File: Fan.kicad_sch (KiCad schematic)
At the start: 0 parts

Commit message: Sheet complete for the fan
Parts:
- added C84, C85: 100nF/50V, A_HDJ_Library:C_0402_1005Metric, symbol Device:C
- added D26, D27: 1N5819WS, A_HDJ_Library:D_SOD-323, symbol Diode:1N5819WS
- added JP79: SolderJumper_2_Open, Jumper:SolderJumper-2_P1.3mm_Bridged_RoundedPad1.0x1.5mm, symbol Jumper:SolderJumper_2_Open
- added M2, M78: Fan_4pin, symbol Motor:Fan_4pin
- added R63: 10k/1%, A_HDJ_Library:R_0402_1005Metric, symbol Device:R
- added R64, R65, R72, R74, R75: 4.7k/1%, A_HDJ_Library:R_0402_1005Metric, symbol Device:R
- added R66, R67, R68, R70: 21.5k/1%, A_HDJ_Library:R_0402_1005Metric, symbol Device:R
- added R69, R71: 100/1%, A_HDJ_Library:R_0402_1005Metric, symbol Device:R
- added R74: 0/1%, Resistor_SMD:R_0201_0603Metric, symbol Device:R
- added TH78: Thermistor_NTC, symbol Device:Thermistor_NTC
- added TP11, TP12: TestPoint, symbol Connector:TestPoint
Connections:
- new net: D26.2 (A), M78.3 (Tacho), R68.2, R72.2
- new net: C85.1, D27.1 (K), M2.2 (+), R74.1, R74.2, R75.2
- new net: D27.2 (A), M2.3 (Tacho), R70.2, R74.2
- new net: JP79.2 (B), R63.1, TH78.1
- new net: M78.4 (PWM), R69.2
- new net: M2.4 (PWM), R71.2
- new net +12V: R75.1
- new net +3.3V: R63.2, R64.2, R65.2
- new net +5V: C84.1, D26.1 (K), M78.2 (+), R72.1, R74.1
- new net FAN_1_PWM: R69.1, TP12.1
- new net FAN_1_TAC: R64.1, R66.2, R68.1, TP11.1
- new net FAN_2_PWM: R71.1
- new net FAN_2_TAC: R65.1, R67.2, R70.1
- new net GND: C84.2, C85.2, M2.1 (-), M78.1 (-), R66.1, R67.1, TH78.2
- new net TEMP: JP79.1 (A)
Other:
- note added: "LattePanda Mu has integrated pull-up resistors (which we will not be using J.S. 2026)"
- note added: "Reserved for 12V fan FAN_TAC input ony allows 3.3v level"

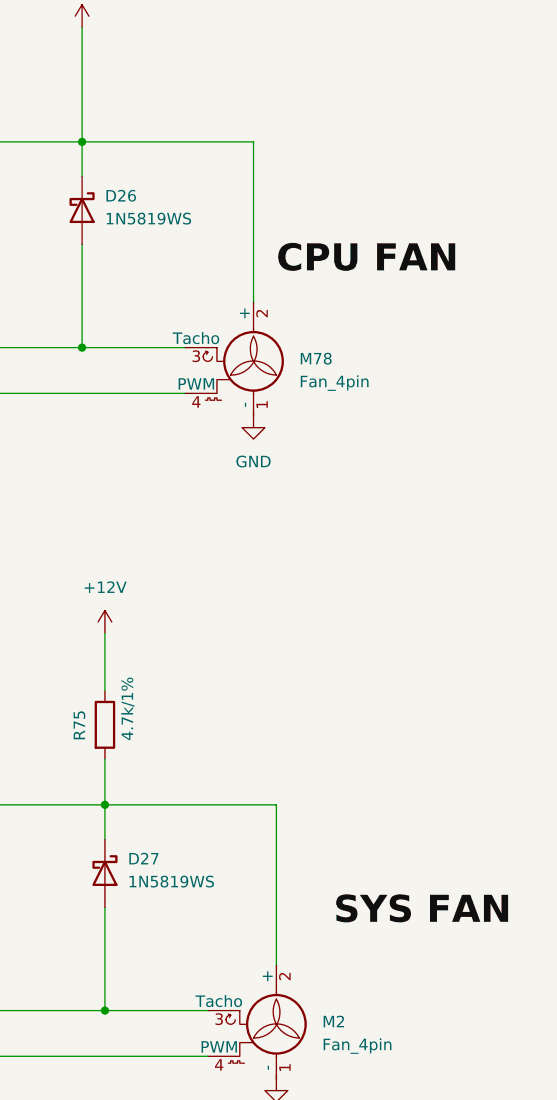
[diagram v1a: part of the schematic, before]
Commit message: Connected the hierarchal sheets together for the fan and the Mu moduls on the main sheet level and also added the label for the extrnal temp sensor for thermistor
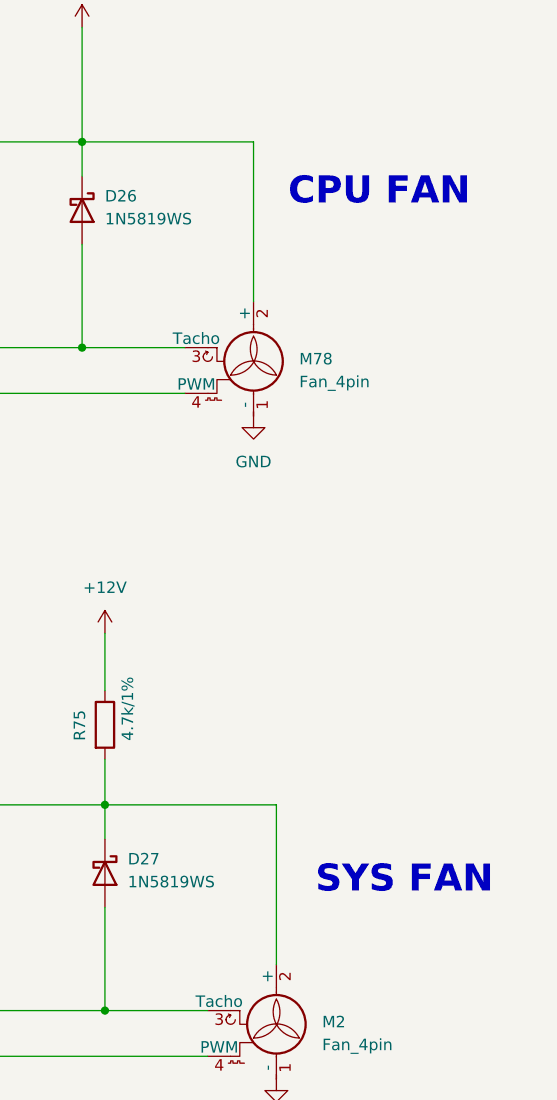
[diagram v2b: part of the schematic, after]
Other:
- note added: "CPU FAN"
- note added: "SYS FAN"
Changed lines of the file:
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@@
+		)
+	)
+	(text "SYS FAN"
+		(exclude_from_sim no)
+		(at 268.224 113.792 0)
+		(effects
+			(font
+				(size 3 3)
+				(thickness 0.6)
+				(bold yes)
+				(color 0 0 255 1)
+			)
 		)
 	)
@@
 			(font
 				(size 1.27 1.27)
+			)
+		)
+	)
+	(text "CPU FAN"
+		(exclude_from_sim no)
+		(at 265.43 37.338 0)
+		(effects
+			(font
+				(size 3 3)
+				(thickness 0.6)
+				(bold yes)
+				(color 0 0 255 1)
 			)
 		)
@@
 		)
 	)
-	(label "SYS FAN"
-		(at 260.35 119.38 0)
-		(effects
-			(font
-				(size 3 3)
-				(thickness 0.6)
-				(bold yes)
-				(color 0 0 255 1)
-			)
-			(justify left bottom)
-		)
-	)
-	(label "CPU FAN"
-		(at 254 46.99 0)
-		(effects
-			(font
-				(size 3 3)
-				(thickness 0.6)
-				(bold yes)
-				(color 0 0 255 1)
-			)
-			(justify left bottom)
-		)
-	)

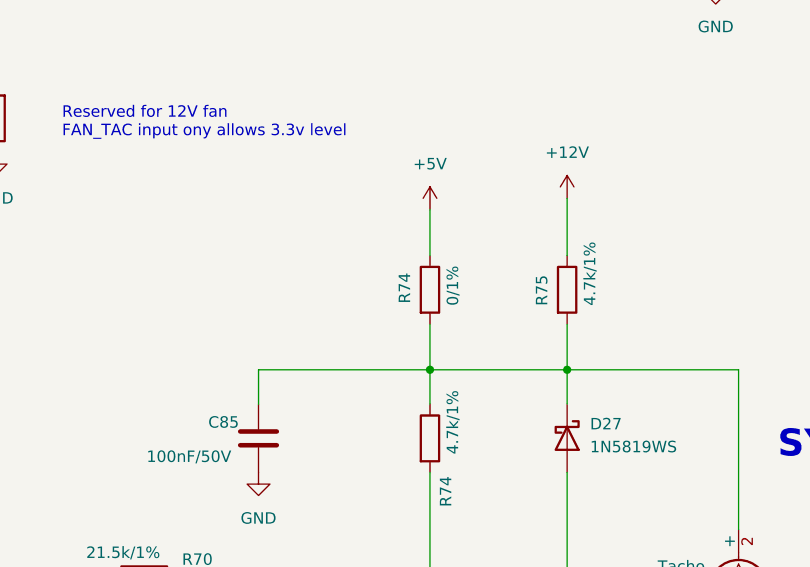
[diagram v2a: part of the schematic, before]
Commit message: Fixed annotation errors duplicate designators on passive components R11 and J15 so that schematic could be imported into pcb. There might be some missing footprints... starting that investigation
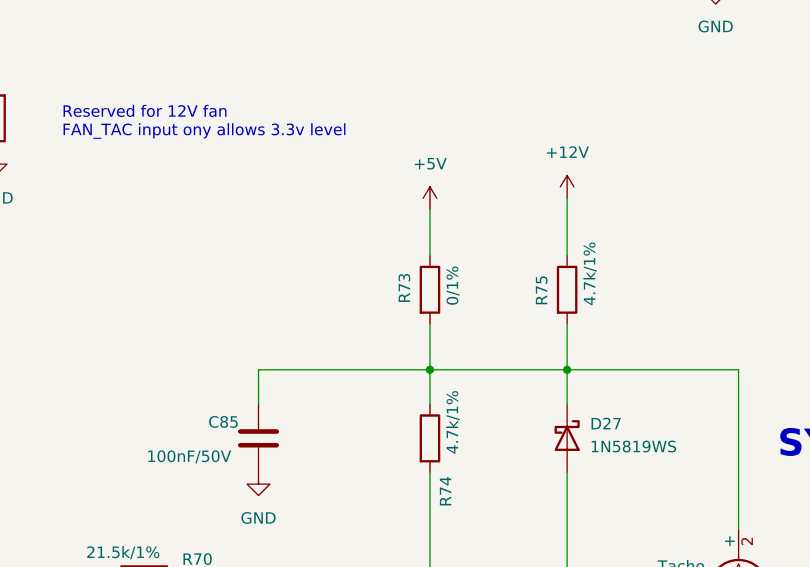
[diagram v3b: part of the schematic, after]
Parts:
- renumbered R74 to R73
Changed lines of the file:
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@@
 		(in_pos_files yes)
 		(dnp no)
-		(property "Reference" "R74"
+		(property "Reference" "R73"
 			(at 216.916 98.044 90)
 			(show_name no)
@@
 			(project "Carrier_Board"
 				(path "/e768274e-12f3-4f83-96f6-abb7638e0bc1/db5534e0-ad9a-443b-b9b9-b696f6fb2c85"
-					(reference "R74")
+					(reference "R73")
 					(unit 1)
 				)

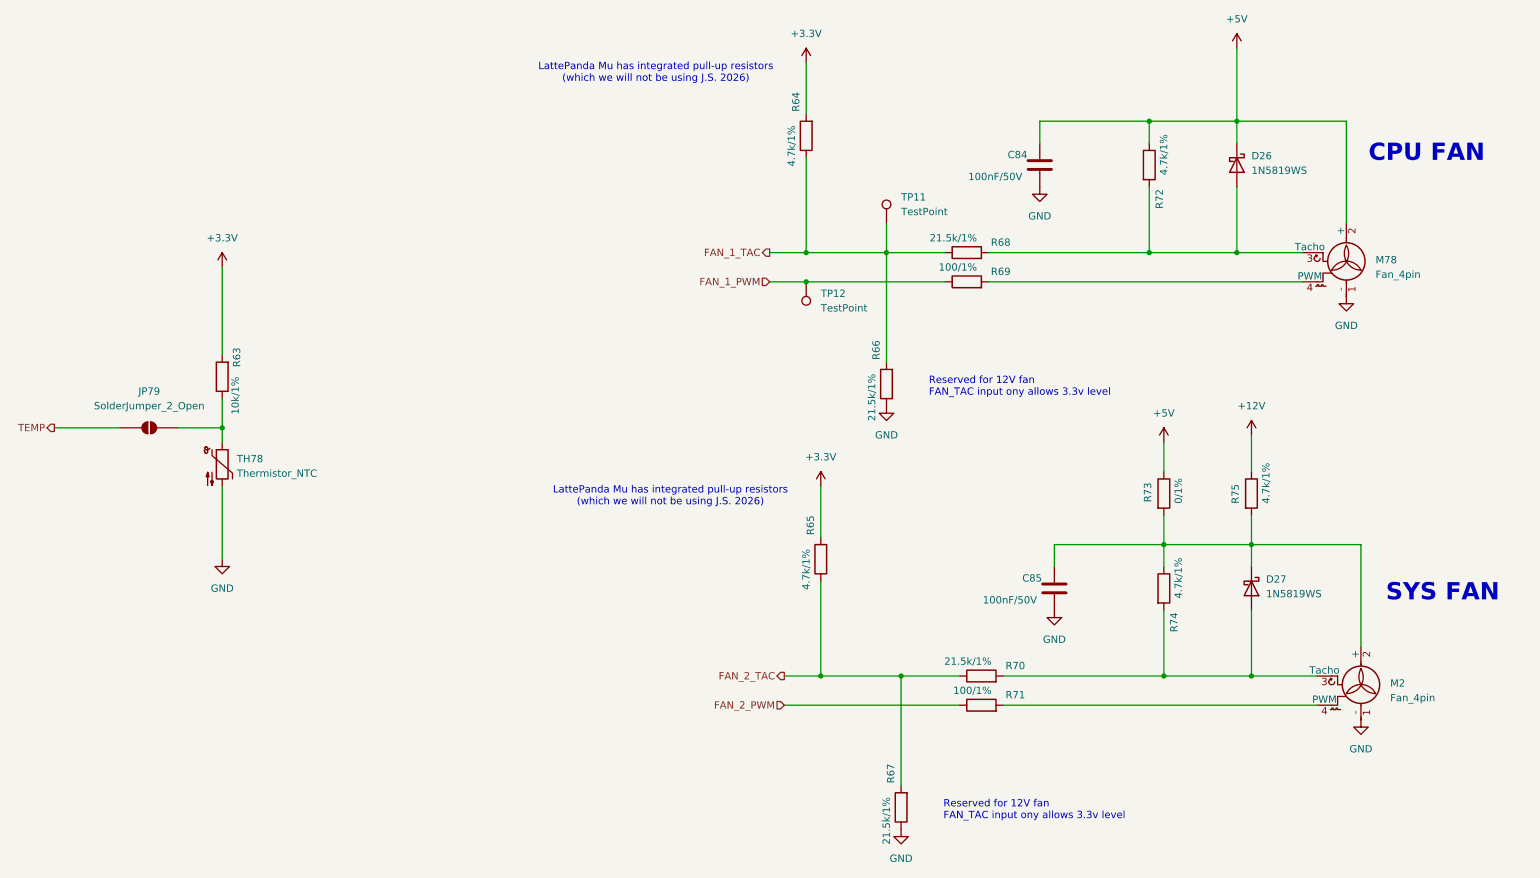
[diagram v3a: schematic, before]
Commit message: Updated all the footprints into the pcb editor but all the designator numbers have changed... I have tp go back and fix each one
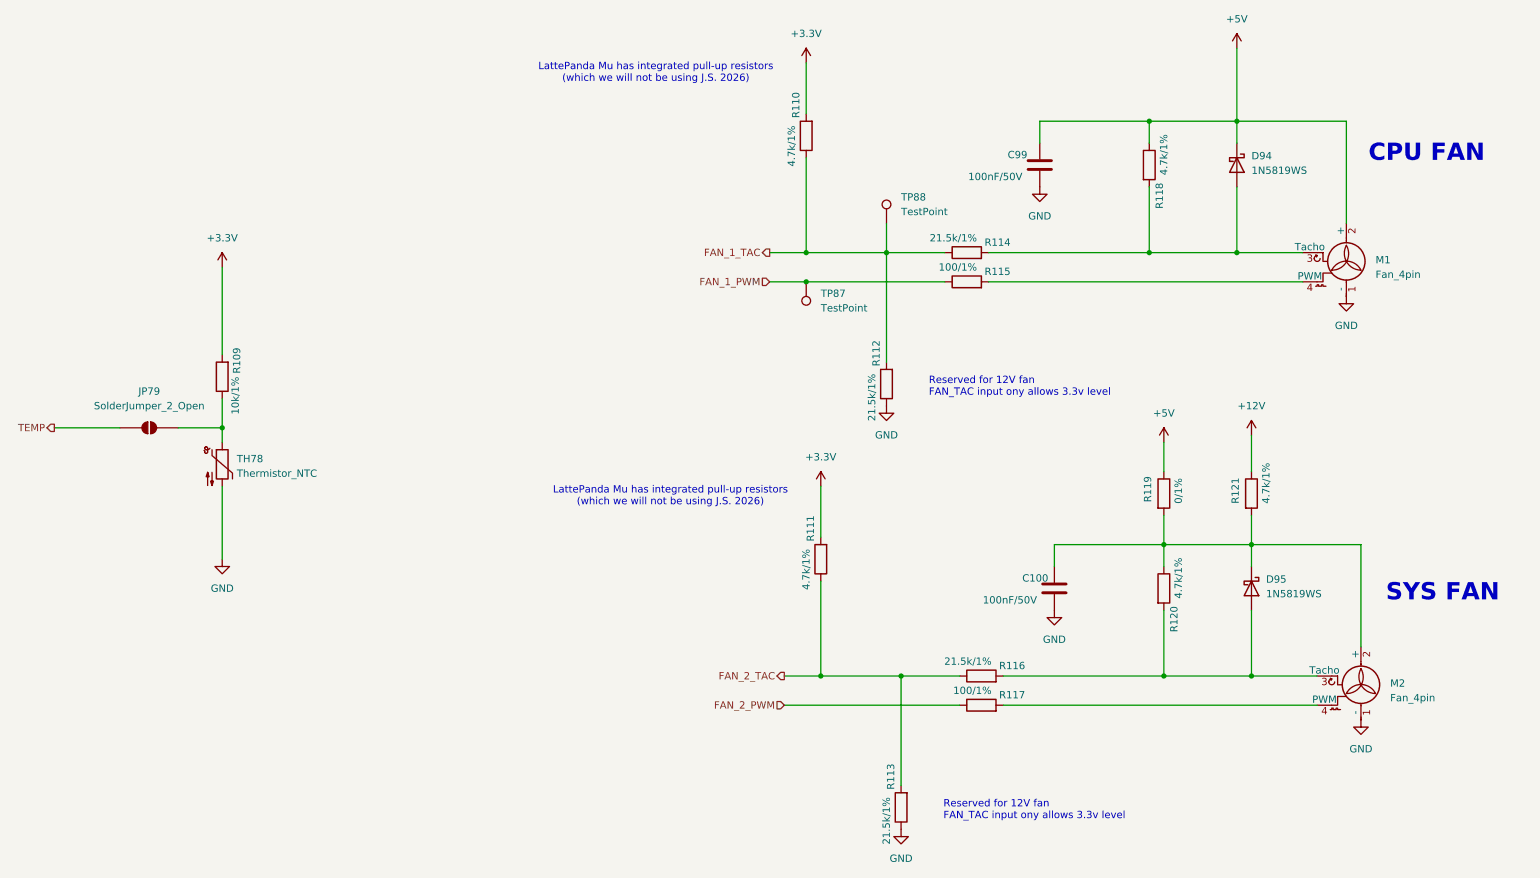
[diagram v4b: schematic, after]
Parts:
- M1: renamed from M78; footprint (none) -> A_HDJ_Library:JST_PH_B4B-PH-K_1x04_P2.00mm_Vertical
- M2: footprint (none) -> A_HDJ_Library:JST_PH_B4B-PH-K_1x04_P2.00mm_Vertical
- TH78: footprint (none) -> A_HDJ_Library:R_0603_1608Metric
- TP87: renamed from TP12; footprint (none) -> A_HDJ_Library:TestPoint_Pad_D1.5mm
- TP88: renamed from TP11; footprint (none) -> A_HDJ_Library:TestPoint_Pad_D1.5mm
- renumbered C85 to C100, C84 to C99, D26 to D94, D27 to D95, R63 to R109, R64 to R110, R65 to R111, R66 to R112, R67 to R113, R68 to R114, R69 to R115, R70 to R116, R71 to R117, R72 to R118, R73 to R119, R74 to R120, R75 to R121

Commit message: Designators in fans restored
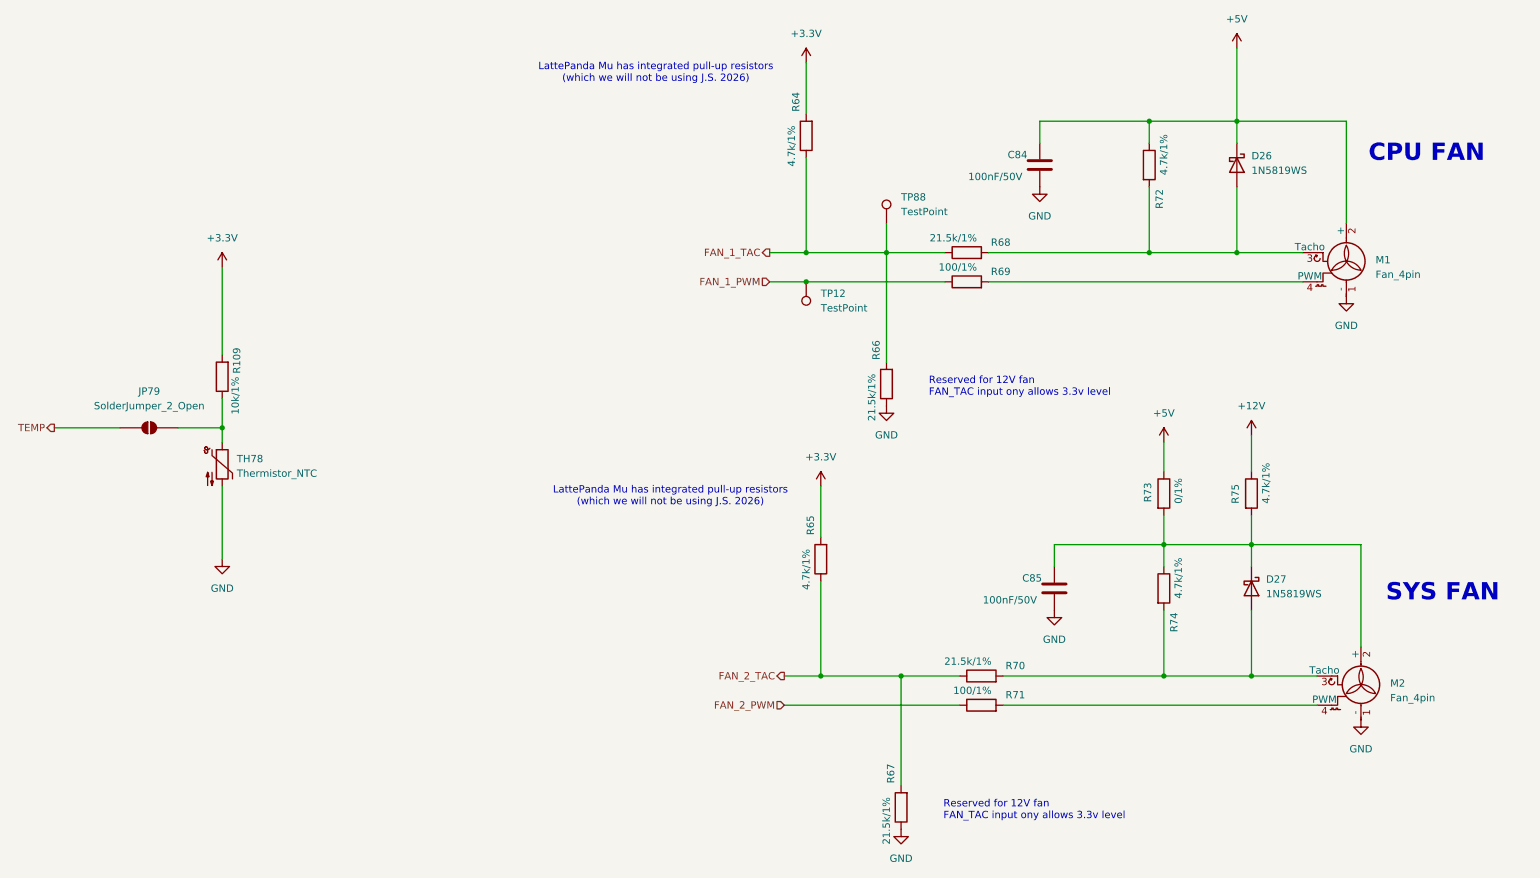
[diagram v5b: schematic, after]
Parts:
- renumbered C99 to C84, C100 to C85, D94 to D26, D95 to D27, R110 to R64, R111 to R65, R112 to R66, R113 to R67, R114 to R68, R115 to R69, R116 to R70, R117 to R71, R118 to R72, R119 to R73, R120 to R74, R121 to R75, TP87 to TP12
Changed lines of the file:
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@@
 		(in_pos_files yes)
 		(dnp no)
-		(property "Reference" "R114"
+		(property "Reference" "R68"
 			(at 193.04 52.832 90)
 			(show_name no)
@@
 			(project "Carrier_Board"
 				(path "/e768274e-12f3-4f83-96f6-abb7638e0bc1/db5534e0-ad9a-443b-b9b9-b696f6fb2c85"
-					(reference "R114")
+					(reference "R68")
 					(unit 1)
 				)
@@
 		(in_pos_files yes)
 		(dnp no)
-		(property "Reference" "R120"
+		(property "Reference" "R74"
 			(at 221.488 120.65 90)
 			(show_name no)
@@
 			(project "Carrier_Board"
 				(path "/e768274e-12f3-4f83-96f6-abb7638e0bc1/db5534e0-ad9a-443b-b9b9-b696f6fb2c85"
-					(reference "R120")
+					(reference "R74")
 					(unit 1)
 				)
@@
 		(in_pos_files yes)
 		(dnp no)
-		(property "Reference" "R113"
+		(property "Reference" "R67"
 			(at 172.212 143.51 90)
 			(show_name no)
@@
 			(project "Carrier_Board"
 				(path "/e768274e-12f3-4f83-96f6-abb7638e0bc1/db5534e0-ad9a-443b-b9b9-b696f6fb2c85"
-					(reference "R113")
+					(reference "R67")
 					(unit 1)
 				)
@@
 		(in_pos_files yes)
 		(dnp no)
-		(property "Reference" "R110"
+		(property "Reference" "R64"
 			(at 155.702 26.67 90)
 			(show_name no)
@@
 			(project "Carrier_Board"
 				(path "/e768274e-12f3-4f83-96f6-abb7638e0bc1/db5534e0-ad9a-443b-b9b9-b696f6fb2c85"
-					(reference "R110")
+					(reference "R64")
 					(unit 1)
 				)
@@
 		(in_pos_files yes)
 		(dnp no)
-		(property "Reference" "R121"
+		(property "Reference" "R75"
 			(at 232.156 98.298 90)
 			(show_name no)
@@
 			(project "Carrier_Board"
 				(path "/e768274e-12f3-4f83-96f6-abb7638e0bc1/db5534e0-ad9a-443b-b9b9-b696f6fb2c85"
-					(reference "R121")
+					(reference "R75")
 					(unit 1)
 				)
@@
 		(in_pos_files yes)
 		(dnp no)
-		(property "Reference" "R111"
+		(property "Reference" "R65"
 			(at 158.242 100.33 90)
 			(show_name no)
@@
 			(project "Carrier_Board"
 				(path "/e768274e-12f3-4f83-96f6-abb7638e0bc1/db5534e0-ad9a-443b-b9b9-b696f6fb2c85"
-					(reference "R111")
+					(reference "R65")
 					(unit 1)
 				)
@@
 		(in_pos_files yes)
 		(dnp no)
-		(property "Reference" "R118"
+		(property "Reference" "R72"
 			(at 218.948 46.99 90)
 			(show_name no)
@@
 			(project "Carrier_Board"
 				(path "/e768274e-12f3-4f83-96f6-abb7638e0bc1/db5534e0-ad9a-443b-b9b9-b696f6fb2c85"
-					(reference "R118")
+					(reference "R72")
 					(unit 1)
 				)
@@
 		(dnp no)
 		(fields_autoplaced yes)
-		(property "Reference" "D94"
+		(property "Reference" "D26"
 			(at 234.95 37.7824 90)
 			(show_name no)
@@
 			(project "Carrier_Board"
 				(path "/e768274e-12f3-4f83-96f6-abb7638e0bc1/db5534e0-ad9a-443b-b9b9-b696f6fb2c85"
-					(reference "D94")
+					(reference "D26")
 					(unit 1)
 				)
@@
 		(in_pos_files yes)
 		(dnp no)
-		(property "Reference" "R116"
+		(property "Reference" "R70"
 			(at 195.58 126.492 90)
 			(show_name no)
@@
 			(project "Carrier_Board"
 				(path "/e768274e-12f3-4f83-96f6-abb7638e0bc1/db5534e0-ad9a-443b-b9b9-b696f6fb2c85"
-					(reference "R116")
+					(reference "R70")
 					(unit 1)
 				)
@@
 		(in_pos_files yes)
 		(dnp no)
-		(property "Reference" "R115"
+		(property "Reference" "R69"
 			(at 193.04 57.912 90)
 			(show_name no)
@@
 			(project "Carrier_Board"
 				(path "/e768274e-12f3-4f83-96f6-abb7638e0bc1/db5534e0-ad9a-443b-b9b9-b696f6fb2c85"
-					(reference "R115")
+					(reference "R69")
 					(unit 1)
 				)
@@
 		(in_pos_files yes)
 		(dnp no)
-		(property "Reference" "C100"
+		(property "Reference" "C85"
 			(at 195.072 111.252 0)
 			(show_name no)
@@
 			(project "Carrier_Board"
 				(path "/e768274e-12f3-4f83-96f6-abb7638e0bc1/db5534e0-ad9a-443b-b9b9-b696f6fb2c85"
-					(reference "C100")
+					(reference "C85")
 					(unit 1)
 				)
@@
 		(in_pos_files yes)
 		(dnp no)
-		(property "Reference" "R119"
+		(property "Reference" "R73"
 			(at 216.916 98.044 90)
 			(show_name no)
@@
 			(project "Carrier_Board"
 				(path "/e768274e-12f3-4f83-96f6-abb7638e0bc1/db5534e0-ad9a-443b-b9b9-b696f6fb2c85"
-					(reference "R119")
+					(reference "R73")
 					(unit 1)
 				)
@@
 		(dnp no)
 		(fields_autoplaced yes)
-		(property "Reference" "TP87"
+		(property "Reference" "TP12"
 			(at 160.02 61.7219 0)
 			(show_name no)
@@
 			(project "Carrier_Board"
 				(path "/e768274e-12f3-4f83-96f6-abb7638e0bc1/db5534e0-ad9a-443b-b9b9-b696f6fb2c85"
-					(reference "TP87")
+					(reference "TP12")
 					(unit 1)
 				)
@@
 		(dnp no)
 		(fields_autoplaced yes)
-		(property "Reference" "D95"
+		(property "Reference" "D27"
 			(at 237.49 111.4424 90)
 			(show_name no)
@@
 			(project "Carrier_Board"
 				(path "/e768274e-12f3-4f83-96f6-abb7638e0bc1/db5534e0-ad9a-443b-b9b9-b696f6fb2c85"
-					(reference "D95")
+					(reference "D27")
 					(unit 1)
 				)
@@
 		(in_pos_files yes)
 		(dnp no)
-		(property "Reference" "R112"
+		(property "Reference" "R66"
 			(at 169.672 69.85 90)
 			(show_name no)
@@
 			(project "Carrier_Board"
 				(path "/e768274e-12f3-4f83-96f6-abb7638e0bc1/db5534e0-ad9a-443b-b9b9-b696f6fb2c85"
-					(reference "R112")
+					(reference "R66")
 					(unit 1)
 				)
@@
 		(in_pos_files yes)
 		(dnp no)
-		(property "Reference" "C99"
+		(property "Reference" "C84"
 			(at 192.532 37.592 0)
 			(show_name no)
@@
 			(project "Carrier_Board"
 				(path "/e768274e-12f3-4f83-96f6-abb7638e0bc1/db5534e0-ad9a-443b-b9b9-b696f6fb2c85"
-					(reference "C99")
+					(reference "C84")
 					(unit 1)
 				)
@@
 		(in_pos_files yes)
 		(dnp no)
-		(property "Reference" "R117"
+		(property "Reference" "R71"
 			(at 195.58 131.572 90)
 			(show_name no)
@@
 			(project "Carrier_Board"
 				(path "/e768274e-12f3-4f83-96f6-abb7638e0bc1/db5534e0-ad9a-443b-b9b9-b696f6fb2c85"
-					(reference "R117")
+					(reference "R71")
 					(unit 1)
 				)
